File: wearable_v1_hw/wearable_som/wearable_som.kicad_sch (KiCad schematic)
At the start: 46 parts, among them IC1 TPS7A0228PDBVR, IC2 DA7280-00FV2, J1 Conn_01x04, J2 USB4105-GF-A, M1 Motor_DC, Q1 PMOS, SW1 Reset, SW2 SW_Nidec_CAS-120A1, SW3 Boot, U1 STM32WB55RGVx, U2 BMI270, U3 MCP73831-2-MC, U4 DLF162500LT-5028A1, U5 2450AT18A100E, U6 USBLC6-2SC6, Y1 Crystal_GND23, Y2 Crystal

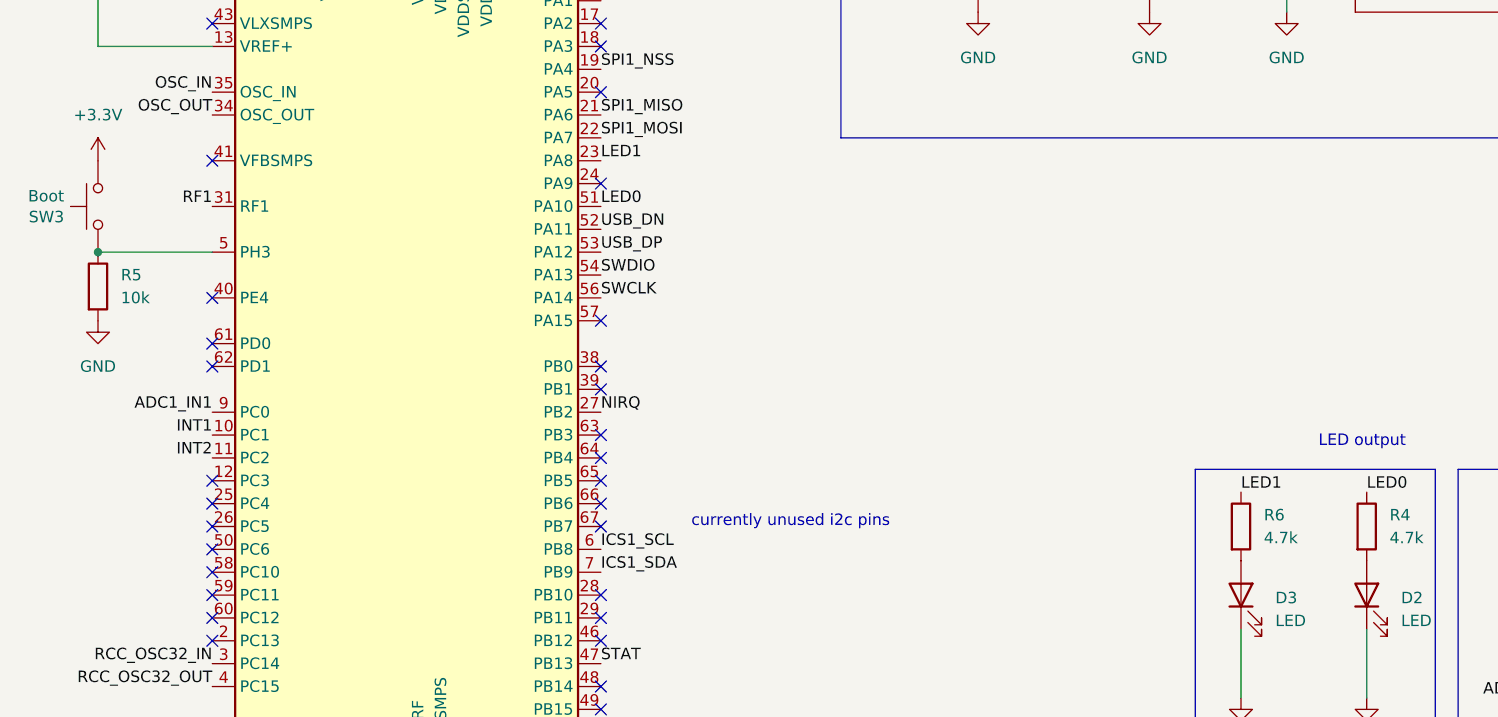
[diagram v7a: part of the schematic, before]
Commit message: final v1 layout done
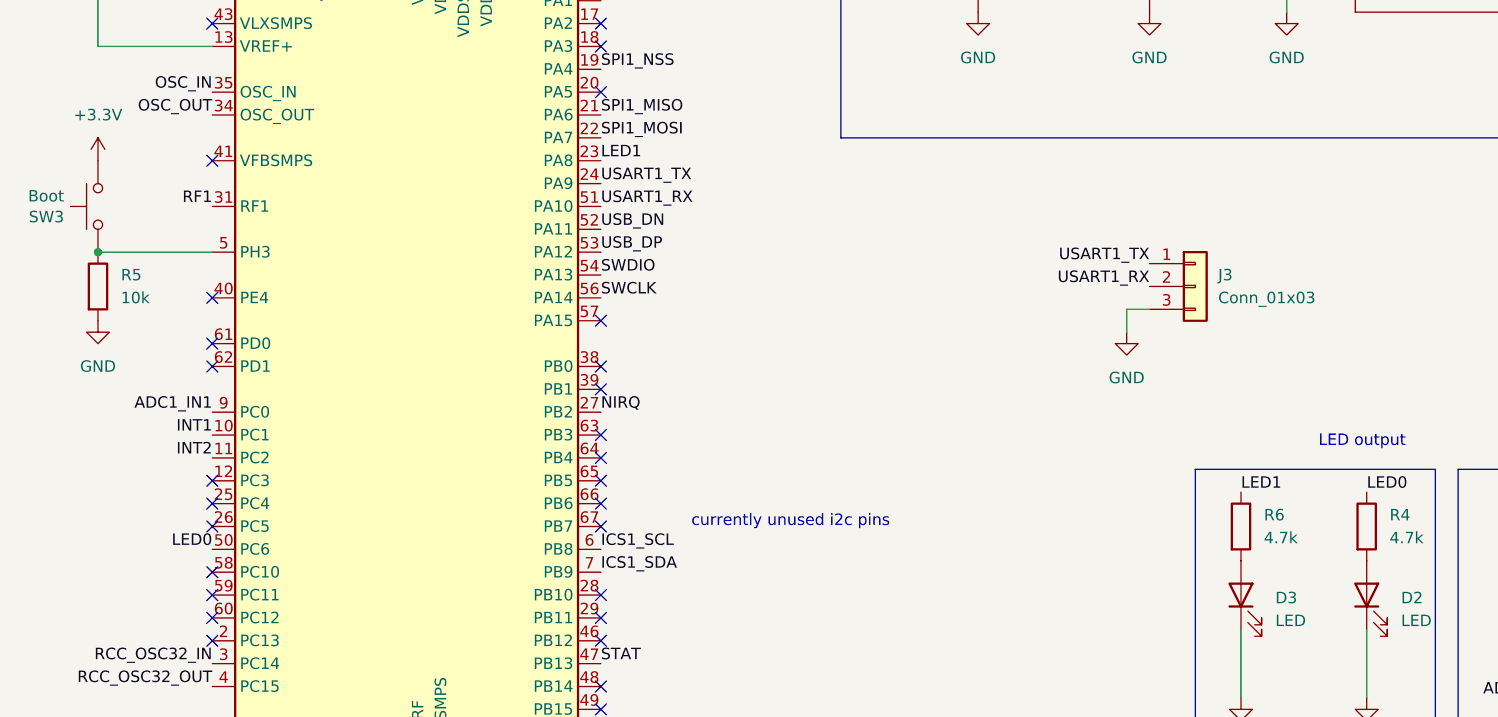
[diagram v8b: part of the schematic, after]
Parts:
- added J3: Conn_01x03, Connector_PinHeader_2.54mm:PinHeader_1x03_P2.54mm_Vertical, symbol Connector_Generic:Conn_01x03
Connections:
- net GND: now also J3.3 (Pin_3)
- net LED0: now also U1.50 (PC6); no longer U1.51 (PA10)
- net USART1_TX: now reaches U1.24 (PA9)
- net USART1_TX: now also J3.1 (Pin_1)
- new net USART1_RX: J3.2 (Pin_2), U1.51 (PA10)
- no-connect marks 41 -> 39
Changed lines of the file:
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@@
-	)
-	(no_connect
-		(at 144.78 173.99)
 	)
 	(no_connect
@@
 	)
 	(no_connect
-		(at 101.6 214.63)
-	)
-	(no_connect
 		(at 299.72 217.17)
 	)
@@
 	(wire
 		(pts
+			(xy 203.2 187.96) (xy 203.2 190.5)
+		)
+		(stroke
+			(width 0)
+			(type default)
+		)
+	)
+	(wire
+		(pts
 			(xy 78.74 83.82) (xy 78.74 82.55)
 		)
@@
 		(pts
 			(xy 38.1 223.52) (xy 38.1 226.06)
+		)
+		(stroke
+			(width 0)
+			(type default)
+		)
+	)
+	(wire
+		(pts
+			(xy 205.74 187.96) (xy 203.2 187.96)
 		)
 		(stroke
@@
 		)
 	)
+	(label "USART1_TX"
+		(at 144.78 173.99 0)
+		(fields_autoplaced yes)
+		(effects
+			(font
+				(size 1.27 1.27)
+			)
+			(justify left bottom)
+		)
+	)
 	(label "DN"
 		(at 73.66 78.74 180)
@@
 		)
 	)
+	(label "USART1_RX"
+		(at 144.78 176.53 0)
+		(fields_autoplaced yes)
+		(effects
+			(font
+				(size 1.27 1.27)
+			)
+			(justify left bottom)
+		)
+	)
 	(label "OSC_IN"
 		(at 62.23 165.1 0)
@@
 		)
 	)
+	(label "USART1_TX"
+		(at 205.74 182.88 180)
+		(fields_autoplaced yes)
+		(effects
+			(font
+				(size 1.27 1.27)
+			)
+			(justify right bottom)
+		)
+	)
 	(label "LED1"
 		(at 215.9 208.28 0)
@@
 		)
 	)
+	(label "USART1_RX"
+		(at 205.74 185.42 180)
+		(fields_autoplaced yes)
+		(effects
+			(font
+				(size 1.27 1.27)
+			)
+			(justify right bottom)
+		)
+	)
 	(label "NRST"
 		(at 50.8 139.7 0)
@@
 	)
 	(label "LED0"
-		(at 144.78 176.53 0)
-		(fields_autoplaced yes)
-		(effects
-			(font
-				(size 1.27 1.27)
-			)
-			(justify left bottom)
+		(at 101.6 214.63 180)
+		(fields_autoplaced yes)
+		(effects
+			(font
+				(size 1.27 1.27)
+			)
+			(justify right bottom)
 		)
 	)
@@
 	)
 	(symbol
+		(lib_name "GND_13")
+		(lib_id "power:GND")
+		(at 203.2 190.5 0)
+		(unit 1)
+		(exclude_from_sim no)
+		(in_bom yes)
+		(on_board yes)
+		(dnp no)
+		(fields_autoplaced yes)
+		(property "Reference" "#PWR048"
+			(at 203.2 196.85 0)
+			(effects
+				(font
+					(size 1.27 1.27)
+				)
+				(hide yes)
+			)
+		)
+		(property "Value" "GND"
+			(at 203.2 195.58 0)
+			(effects
+				(font
+					(size 1.27 1.27)
+				)
+			)
+		)
+		(property "Footprint" ""
+			(at 203.2 190.5 0)
+			(effects
+				(font
+					(size 1.27 1.27)
+				)
+				(hide yes)
+			)
+		)
+		(property "Datasheet" ""
+			(at 203.2 190.5 0)
+			(effects
+				(font
+					(size 1.27 1.27)
+				)
+				(hide yes)
+			)
+		)
+		(property "Description" "Power symbol creates a global label with name \"GND\" , ground"
+			(at 203.2 190.5 0)
+			(effects
+				(font
+					(size 1.27 1.27)
+				)
+				(hide yes)
+			)
+		)
+		(pin "1"
+		)
+		(instances
+			(project ""
+				(path "/2b3d3954-12cd-497b-89a5-937375044fa2"
+					(reference "#PWR048")
+					(unit 1)
+				)
+			)
+		)
+	)
+	(symbol
 		(lib_id "power:+3.3VA")
 		(at 114.935 26.035 0)
@@
 					(unit 1)
 				)
+			)
+		)
+	)
+	(symbol
+		(lib_id "Connector_Generic:Conn_01x03")
+		(at 210.82 185.42 0)
+		(unit 1)
+		(exclude_from_sim no)
+		(in_bom yes)
+		(on_board yes)
+		(dnp no)
+		(fields_autoplaced yes)
+		(property "Reference" "J3"
+			(at 213.36 184.1499 0)
+			(effects
+				(font
+					(size 1.27 1.27)
+				)
+				(justify left)
+			)
+		)
+		(property "Value" "Conn_01x03"
+			(at 213.36 186.6899 0)
+			(effects
+				(font
+					(size 1.27 1.27)
+				)
+				(justify left)
+			)
+		)
+		(property "Footprint" "Connector_PinHeader_2.54mm:PinHeader_1x03_P2.54mm_Vertical"
+			(at 210.82 185.42 0)
+			(effects
+				(font
+					(size 1.27 1.27)
+				)
+				(hide yes)
+			)
+		)
+		(property "Datasheet" "~"
+			(at 210.82 185.42 0)
+			(effects
+				(font
+					(size 1.27 1.27)
+				)
+				(hide yes)
+			)
+		)
+		(property "Description" "Generic connector, single row, 01x03, script generated (kicad-library-utils/schlib/autogen/connector/)"
+			(at 210.82 185.42 0)
+			(effects
+				(font
+					(size 1.27 1.27)
+				)
+				(hide yes)
+			)
+		)
+		(pin "1"
+		)
+		(pin "2"
+		)
+		(pin "3"
+		)
+		(instances
+			(project ""
+				(path "/2b3d3954-12cd-497b-89a5-937375044fa2"
+					(reference "J3")
+					(unit 1)
+				)
